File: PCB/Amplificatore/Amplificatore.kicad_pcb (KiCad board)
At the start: 2 copper layers, 11 parts, among them U2 ECC83

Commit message: avanzamento pcb
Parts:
- added C10: 680nF, Capacitor_THT:C_Rect_L18.0mm_W11.0mm_P15.00mm_FKS3_FKP3, F.Cu at (212.1, 97.6)
- added C11: 22nF, Capacitor_THT:C_Rect_L13.0mm_W4.0mm_P10.00mm_FKS3_FKP3_MKS4, F.Cu at (212.1, 112.2)
- added C5: 22nF, Capacitor_THT:C_Rect_L13.0mm_W4.0mm_P10.00mm_FKS3_FKP3_MKS4, F.Cu at (212.1, 106.7)
- added C7: 1nF, Capacitor_THT:C_Rect_L13.0mm_W4.0mm_P10.00mm_FKS3_FKP3_MKS4, F.Cu at (231.6, 94.1)
- added C8: 10uF, Capacitor_Tantalum_SMD:CP_EIA-3216-10_Kemet-I, F.Cu at (227.2, 110.0)
- added C9: 470pF, Capacitor_THT:C_Rect_L10.0mm_W3.0mm_P7.50mm_MKS4, F.Cu at (226.4, 106.2)
- added J1: POT-1, Connector_PinSocket_2.00mm:PinSocket_1x03_P2.00mm_Vertical, F.Cu at (237.9, 103.8)
- added R6: 100K, Resistor_SMD:R_2512_6332Metric, F.Cu at (233.7, 99.3)
- added R7: 1K5, Resistor_SMD:R_0805_2012Metric, F.Cu at (232.3, 109.9)
- added R8: 100K, Resistor_SMD:R_2512_6332Metric, F.Cu at (248.3, 93.8)
- added R9: 47K, Resistor_SMD:R_2512_6332Metric, F.Cu at (242.4, 99.3)
- renumbered C3 to C2, C5 to C3, C2 to C4, C4 to C6, R4 to R3, R3 to R4, U2 to U1
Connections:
- U1 pad 1: (no net) -> Net-(C11-Pad2)
- U1 pad 2: (no net) -> Net-(R6-Pad1)
- U1 pad 3: (no net) -> Net-(C10-Pad2)

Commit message: Add files via upload
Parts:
- added K1: G5Q-1, Relay_THT:Relay_SPDT_Omron-G5Q-1, F.Cu at (226.1, 73.7)
- added R10: 220K, Resistor_SMD:R_2512_6332Metric, F.Cu at (227.9, 78.6)
- added R11: 220K, Resistor_SMD:R_2512_6332Metric, F.Cu at (236.6, 78.6)
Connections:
- R4 pad 1: Net-(C2-Pad1) -> Net-(C6-Pad1)

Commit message: ...
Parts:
- added C12: 1nF, Capacitor_THT:C_Rect_L13.0mm_W4.0mm_P10.00mm_FKS3_FKP3_MKS4, F.Cu at (137.2, 73.7)
- added C13: 2n2F, Capacitor_THT:C_Rect_L13.0mm_W4.0mm_P10.00mm_FKS3_FKP3_MKS4, F.Cu at (130.8, 81.3)
- added C14: 100nF, Capacitor_THT:C_Rect_L18.0mm_W5.0mm_P15.00mm_FKS3_FKP3, F.Cu at (160.0, 82.5)
- added C15: 100nF, Capacitor_THT:C_Rect_L18.0mm_W5.0mm_P15.00mm_FKS3_FKP3, F.Cu at (181.6, 63.5)
- added C16: 100nF, Capacitor_THT:C_Rect_L18.0mm_W5.0mm_P15.00mm_FKS3_FKP3, F.Cu at (186.7, 50.8)
- added C17: 4n7F, Capacitor_THT:C_Rect_L13.0mm_W4.0mm_P10.00mm_FKS3_FKP3_MKS4, F.Cu at (186.7, 57.1)
- added C18: 10nF, Capacitor_THT:C_Rect_L13.0mm_W4.0mm_P10.00mm_FKS3_FKP3_MKS4, F.Cu at (221.0, 57.1)
- added C19: 220pF, Capacitor_THT:C_Rect_L7.2mm_W4.5mm_P5.00mm_FKS2_FKP2_MKS2_MKP2, F.Cu at (203.2, 64.8)
- added C20: 470pF, Capacitor_THT:C_Rect_L10.0mm_W3.0mm_P7.50mm_MKS4, F.Cu at (219.7, 63.5)
- added C21: 100nF, Capacitor_THT:C_Rect_L18.0mm_W5.0mm_P15.00mm_FKS3_FKP3, F.Cu at (210.8, 50.8)
- added C22: 2n2F, Capacitor_THT:C_Rect_L13.0mm_W4.0mm_P10.00mm_FKS3_FKP3_MKS4, F.Cu at (233.7, 69.8)
- added D1: 1N4007, Diode_THT:D_DO-41_SOD81_P10.16mm_Horizontal, F.Cu at (135.9, 58.4)
- added D2: 1N4007, Diode_THT:D_DO-41_SOD81_P10.16mm_Horizontal, F.Cu at (148.6, 58.4)
- added D3: 1N4007, Diode_THT:D_DO-41_SOD81_P10.16mm_Horizontal, F.Cu at (143.5, 73.7)
- added D4: 1N4007, Diode_THT:D_DO-41_SOD81_P10.16mm_Horizontal, F.Cu at (142.2, 48.3)
- added D5: 1N4007, Diode_THT:D_DO-41_SOD81_P10.16mm_Horizontal, F.Cu at (129.5, 48.3)
- added D6: 1N4007, Diode_THT:D_DO-41_SOD81_P10.16mm_Horizontal, F.Cu at (143.5, 81.3)
- added D7: 1N4007, Diode_THT:D_DO-41_SOD81_P10.16mm_Horizontal, F.Cu at (137.2, 91.4)
- added J10: POWER, Connector_Molex:Molex_KK-396_A-41791-0003_1x03_P3.96mm_Vertical, F.Cu at (109.2, 47.0)
- added J11: FILAMENT-U2, Connector_PinSocket_2.00mm:PinSocket_1x03_P2.00mm_Vertical, F.Cu at (166.4, 54.6)
- added J12: FILAMENT-U1, Connector_PinSocket_2.00mm:PinSocket_1x03_P2.00mm_Vertical, F.Cu at (99.1, 55.9)
- added J2: POT-LEAD, Connector_PinSocket_2.00mm:PinSocket_1x03_P2.00mm_Vertical, F.Cu at (129.5, 67.3)
- added J3: SEND-RETURN, Connector_PinSocket_2.00mm:PinSocket_1x03_P2.00mm_Vertical, F.Cu at (184.2, 76.2)
- added J4: In, Connector_PinSocket_2.00mm:PinSocket_1x03_P2.00mm_Vertical, F.Cu at (53.3, 64.8)
- added J5: POT-BASS-BACK, Connector_PinSocket_2.00mm:PinSocket_1x03_P2.00mm_Vertical, F.Cu at (193.0, 49.5)
- added J6: POT-MID, Connector_PinSocket_2.00mm:PinSocket_1x03_P2.00mm_Vertical, F.Cu at (214.6, 63.5)
- added J7: POT-TREBLE, Connector_PinSocket_2.00mm:PinSocket_1x03_P2.00mm_Vertical, F.Cu at (221.0, 72.4)
- added J8: POT-BASS-FRONT, Connector_PinSocket_2.00mm:PinSocket_1x03_P2.00mm_Vertical, F.Cu at (224.8, 78.7)
- added J9: MASTER, Connector_PinSocket_2.00mm:PinSocket_1x03_P2.00mm_Vertical, F.Cu at (224.8, 85.1)
- added K2: G5Q-1, Relay_THT:Relay_SPDT_Omron-G5Q-1, F.Cu at (102.9, 90.2)
- added K3: G5Q-1, Relay_THT:Relay_SPDT_Omron-G5Q-1, F.Cu at (190.5, 72.4)
- added K4: G5Q-1, Relay_THT:Relay_SPDT_Omron-G5Q-1, F.Cu at (204.5, 72.4)
- added R12: 10K, Resistor_SMD:R_2512_6332Metric, F.Cu at (151.1, 71.1)
- added R13: 100K, Resistor_SMD:R_2512_6332Metric, F.Cu at (151.1, 81.3)
- added R14: 47K, Resistor_SMD:R_2512_6332Metric, F.Cu at (152.4, 63.5)
- added R15: 1Meg, Resistor_SMD:R_0805_2012Metric, F.Cu at (158.8, 90.2)
- added R16: 1K5, Resistor_SMD:R_0805_2012Metric, F.Cu at (156.2, 58.4)
- added R17: 100K, Resistor_SMD:R_2512_6332Metric, B.Cu at (154.9, 50.8)
- added R18: 47K, Resistor_SMD:R_2512_6332Metric, F.Cu at (151.1, 90.2)
- added R19: 100K, Resistor_SMD:R_2512_6332Metric, F.Cu at (166.4, 90.2)
- added R20: 10K, Resistor_SMD:R_2512_6332Metric, F.Cu at (176.5, 90.2)
- added R21: 10R, Resistor_SMD:R_2512_6332Metric, F.Cu at (184.2, 88.1)
- added R22: 1Meg, Resistor_SMD:R_0805_2012Metric, B.Cu at (189.2, 63.5)
- added R23: 470R, Resistor_SMD:R_0805_2012Metric, F.Cu at (180.3, 74.6)
- added R24: 220K, Resistor_SMD:R_2512_6332Metric, F.Cu at (163.8, 48.3)
- added R25: 100K, Resistor_SMD:R_2512_6332Metric, F.Cu at (199.4, 52.1)
- added R26: 100K, Resistor_SMD:R_2512_6332Metric, F.Cu at (204.5, 52.1)
- added R27: 10K, Resistor_SMD:R_2512_6332Metric, F.Cu at (233.7, 52.1)
- added R28: 100K, Resistor_SMD:R_2512_6332Metric, F.Cu at (233.7, 77.5)
- added U2: ECC83, Valve:Valve_ECC-83-2, B.Cu at (171.4, 63.5)
- C8, R1, R3, R7, R9, U1: moved to B.Cu
- J1: value POT-1 -> POT-GAIN
- moved J1 186.7 mm to (53.3, 76.2), turned to 180 degrees
- moved C7 173.3 mm to (58.4, 88.9)
- moved R8 171.0 mm to (81.3, 57.1)
- moved C9 161.6 mm to (73.7, 53.3), turned to 180 degrees
- moved R6 159.2 mm to (74.9, 87.6), turned to 270 degrees
- moved C5 155.6 mm to (58.4, 82.5)
- moved R11 149.4 mm to (87.6, 90.2)
- moved R10 140.4 mm to (87.6, 83.8), turned to 180 degrees
- moved C4 133.8 mm to (58.4, 72.4)
- moved R9 132.7 mm to (110.5, 85.1), turned to 180 degrees
- moved R7 128.4 mm to (113.0, 62.2)
- moved C8 125.9 mm to (113.0, 57.1)
- moved K1 123.2 mm to (102.9, 76.2)
- moved C11 117.7 mm to (96.5, 90.2), turned to 90 degrees
- moved C1 105.1 mm to (58.4, 63.5), turned to 90 degrees
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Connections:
- net LEAD-SW-A renamed LEAD-SW
- net Net-(C5-Pad1) renamed /Mute
- C6 pad 1: Net-(C6-Pad1) -> /VCC
- C9 pad 2: Net-(C6-Pad1) -> Net-(C2-Pad1)
- K1 pad 2: Net-(K1-Pad2) -> GND
- K1 pad 5: LEAD-SW-B -> COMMON
- R4 pad 1: Net-(C6-Pad1) -> Net-(C2-Pad1)
- R5 pad 1: Net-(C6-Pad1) -> /VCC
- R8 pad 1: Net-(C6-Pad1) -> Net-(C2-Pad1)
- U1 pad 4: (no net) -> Net-(J12-Pad1)
- U1 pad 5: (no net) -> Net-(J12-Pad2)
- U1 pad 9: (no net) -> Net-(J12-Pad3)

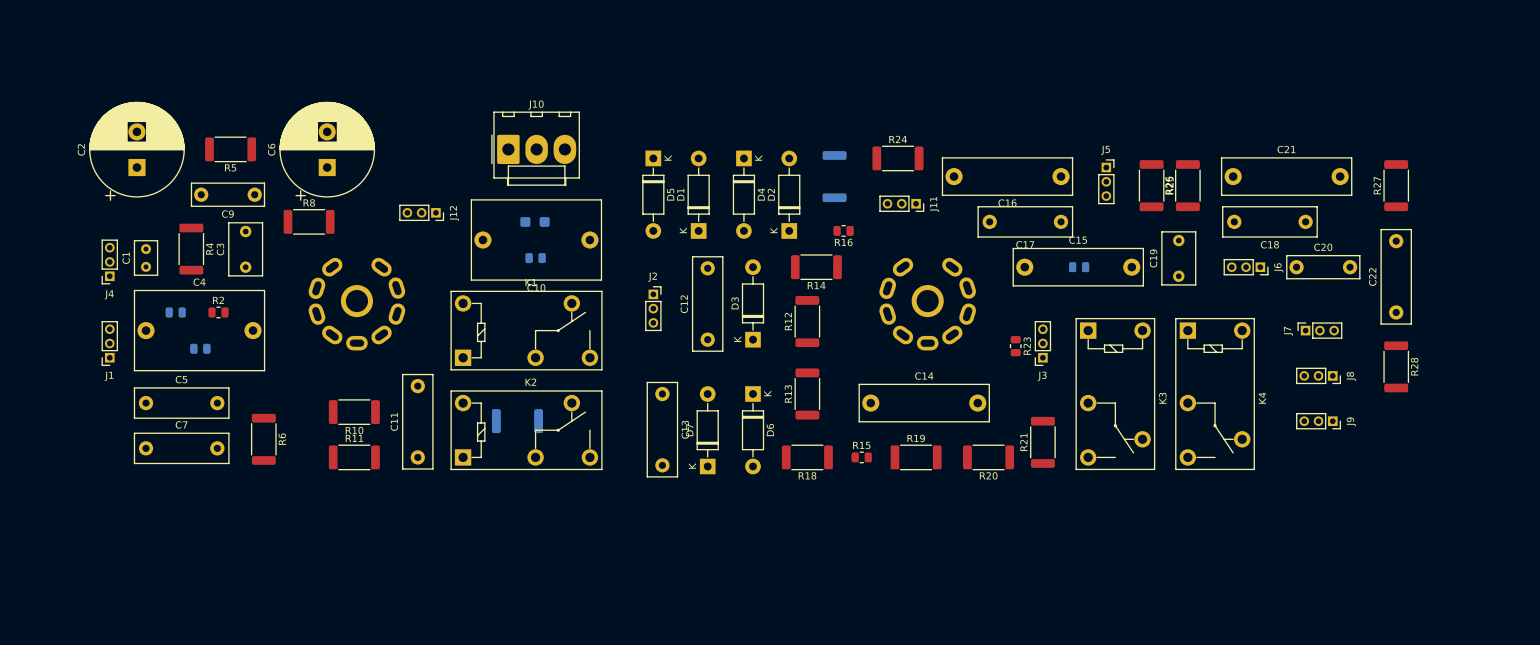
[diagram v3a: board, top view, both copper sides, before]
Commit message: sbrogliato pcb pre-ampli
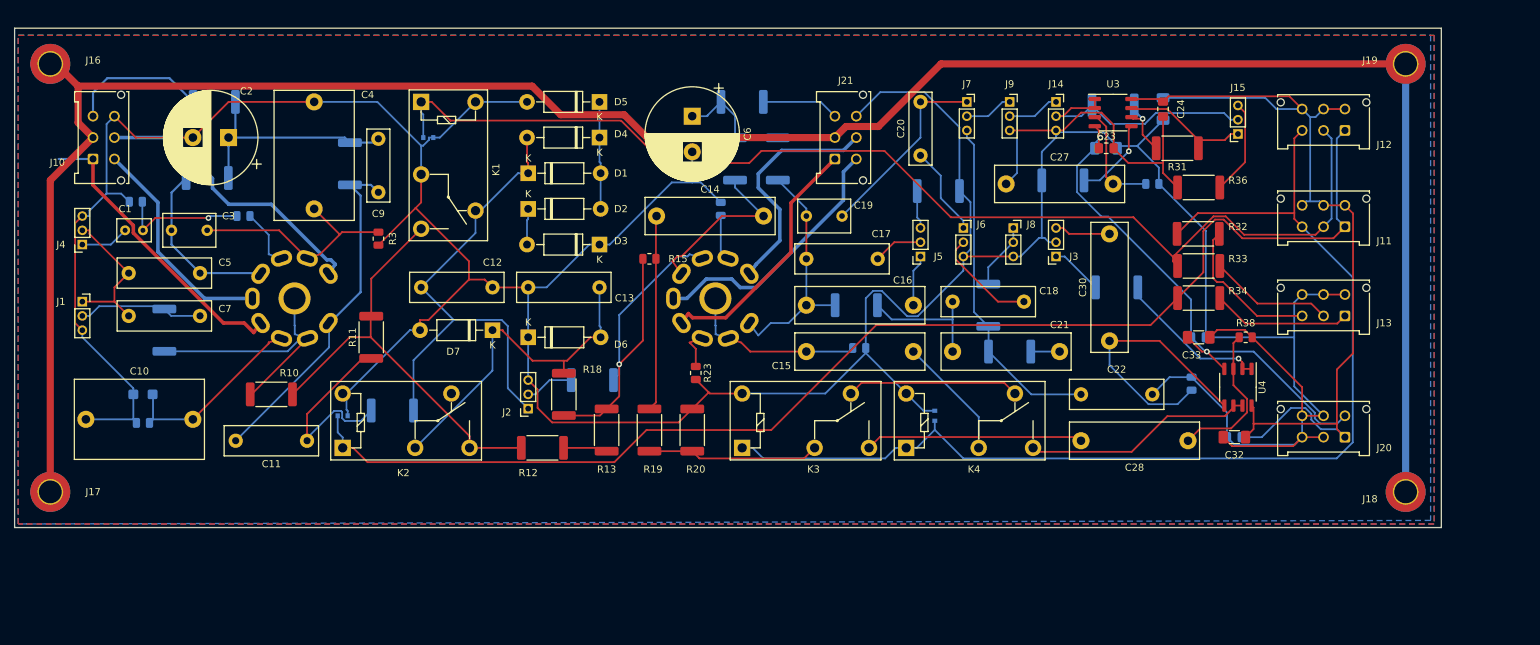
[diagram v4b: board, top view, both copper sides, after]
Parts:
- added C23: 100nF, Capacitor_SMD:C_0805_2012Metric_Pad1.18x1.45mm_HandSolder, F.Cu at (193.0, 46.8)
- added C24: 100nF, Capacitor_SMD:C_0805_2012Metric_Pad1.18x1.45mm_HandSolder, F.Cu at (201.0, 41.3)
- added C25: 1uF, Capacitor_SMD:C_1206_3216Metric_Pad1.33x1.80mm_HandSolder, B.Cu at (201.0, 41.3)
- added C26: 1uF, Capacitor_SMD:C_1206_3216Metric_Pad1.33x1.80mm_HandSolder, B.Cu at (193.0, 46.8)
- added C27: 100nF, Capacitor_THT:C_Rect_L18.0mm_W5.0mm_P15.00mm_FKS3_FKP3, F.Cu at (179.0, 51.8)
- added C28: 100nF, Capacitor_THT:C_Rect_L18.0mm_W5.0mm_P15.00mm_FKS3_FKP3, F.Cu at (204.5, 87.8)
- added C29: 100nF, Capacitor_SMD:C_0805_2012Metric_Pad1.18x1.45mm_HandSolder, B.Cu at (206.0, 73.3)
- added C30: 100nF, Capacitor_THT:C_Rect_L18.0mm_W5.0mm_P15.00mm_FKS3_FKP3, F.Cu at (193.5, 73.8)
- added C31: 100nF, Capacitor_SMD:C_0805_2012Metric_Pad1.18x1.45mm_HandSolder, B.Cu at (211.0, 87.3)
- added C32: 1uF, Capacitor_SMD:C_1206_3216Metric_Pad1.33x1.80mm_HandSolder, F.Cu at (211.0, 87.3)
- added C33: 1uF, Capacitor_SMD:C_1206_3216Metric_Pad1.33x1.80mm_HandSolder, F.Cu at (206.0, 73.3)
- added D10: 1N4148WT, Diode_SMD:D_SOD-523, B.Cu at (169.0, 84.3)
- added D8: 1N4148WT, Diode_SMD:D_SOD-523, B.Cu at (86.0, 84.3)
- added D9: 1N4148WT, Diode_SMD:D_SOD-523, B.Cu at (98.0, 45.3)
- added J13: LED_SWITCHES, Connector_Molex:Molex_Micro-Fit_3.0_43045-0612_2x03_P3.00mm_Vertical, F.Cu at (226.5, 70.3)
- added J14: POWER-STAGE, Connector_PinSocket_2.00mm:PinSocket_1x03_P2.00mm_Vertical, F.Cu at (186.0, 40.3)
- added J15: LINE-OUT, Connector_PinSocket_2.00mm:PinSocket_1x03_P2.00mm_Vertical, F.Cu at (211.5, 44.8)
- added J16: Conn_01x01, MountingHole:MountingHole_3.2mm_M3_DIN965_Pad_TopBottom, F.Cu at (45.0, 35.0)
- added J17: Conn_01x01, MountingHole:MountingHole_3.2mm_M3_DIN965_Pad_TopBottom, F.Cu at (45.0, 95.0)
- added J18: Conn_01x01, MountingHole:MountingHole_3.2mm_M3_DIN965_Pad_TopBottom, F.Cu at (235.0, 95.0)
- added J19: Conn_01x01, MountingHole:MountingHole_3.2mm_M3_DIN965_Pad_TopBottom, F.Cu at (235.0, 35.0)
- added J20: PWR_DC, Connector_Molex:Molex_Micro-Fit_3.0_43045-0612_2x03_P3.00mm_Vertical, F.Cu at (226.5, 87.3)
- added J21: PWR_VALVE2, Connector_Molex:Molex_Micro-Fit_3.0_43045-0612_2x03_P3.00mm_Vertical, F.Cu at (155.0, 48.3)
- added R29: 100K, Resistor_SMD:R_2512_6332Metric, B.Cu at (194.0, 40.8)
- added R30: 10K, Resistor_SMD:R_2512_6332Metric, B.Cu at (187.0, 51.3)
- added R31: 10K, Resistor_SMD:R_2512_6332Metric, F.Cu at (203.0, 46.8)
- added R32: 1K, Resistor_SMD:R_2512_6332Metric, F.Cu at (205.9, 58.8)
- added R33: 1K, Resistor_SMD:R_2512_6332Metric, F.Cu at (206.0, 63.3)
- added R34: 1K, Resistor_SMD:R_2512_6332Metric, F.Cu at (206.0, 67.8)
- added R35: 1Meg, Resistor_SMD:R_0805_2012Metric, B.Cu at (199.5, 51.8)
- added R36: 10R, Resistor_SMD:R_2512_6332Metric, F.Cu at (206.0, 52.3)
- added R37: 10K, Resistor_SMD:R_2512_6332Metric, B.Cu at (68.0, 40.3)
- added R38: 1Meg, Resistor_SMD:R_0805_2012Metric, F.Cu at (212.6, 73.3)
- added R39: 1Meg, Resistor_SMD:R_0805_2012Metric, B.Cu at (205.0, 79.8)
- added U3: TL082, Package_SO:SO-8_3.9x4.9mm_P1.27mm, F.Cu at (194.0, 41.8)
- added U4: TL082, Package_SO:SO-8_3.9x4.9mm_P1.27mm, F.Cu at (211.5, 80.3)
- J10: value POWER -> PWR_VALVE1; footprint Connector_Molex:Molex_KK-396_A-41791-0003_1x03_P3.96mm_Vertical -> Connector_Molex:Molex_Micro-Fit_3.0_43045-0612_2x03_P3.00mm_Vertical
- J11: value FILAMENT-U2 -> LOCAL_SWITCHES; footprint Connector_PinSocket_2.00mm:PinSocket_1x03_P2.00mm_Vertical -> Connector_Molex:Molex_Micro-Fit_3.0_43045-0612_2x03_P3.00mm_Vertical
- J12: value FILAMENT-U1 -> REMOTE_SWITCHES; footprint Connector_PinSocket_2.00mm:PinSocket_1x03_P2.00mm_Vertical -> Connector_Molex:Molex_Micro-Fit_3.0_43045-0612_2x03_P3.00mm_Vertical
- R14, R16, R2, R21, R24, R25, R26, R27, R28, R4, R5, R6, R8: moved to B.Cu
- R3: moved to F.Cu
- moved J12 128.0 mm to (226.5, 44.3), turned to 180 degrees
- moved C10 75.0 mm to (50.0, 84.8), turned to 0 degrees
- moved R5 72.0 mm to (142.0, 40.3), turned to 0 degrees
- moved J9 63.7 mm to (179.5, 40.3), turned to 0 degrees
- moved J11 60.2 mm to (226.5, 57.8), turned to 180 degrees
- moved C8 60.0 mm to (58.0, 81.3), turned to 180 degrees
- moved R7 59.7 mm to (58.0, 85.3), turned to 180 degrees
- moved R27 59.0 mm to (179.5, 75.3), turned to 0 degrees
- moved J10 58.2 mm to (51.0, 48.3), turned to 90 degrees
- moved R28 57.8 mm to (176.5, 68.8), turned to 90 degrees
- moved J7 57.3 mm to (173.5, 40.3), turned to 0 degrees
- moved C20 55.0 mm to (167.0, 47.8), turned to 90 degrees
- moved C6 51.7 mm to (135.0, 42.3), turned to 270 degrees
- moved K3 51.2 mm to (142.0, 88.8), turned to 0 degrees
- moved R26 49.4 mm to (158.0, 68.8), turned to 0 degrees
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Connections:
- C6 pad 1: /VCC -> /VCC2_B
- J10 pad 1: /VCC -> Net-(J10-Pad1)
- J10 pad 3: GND -> /VCC1
- J11 pad 1: Net-(J11-Pad1) -> /RITHM-SW
- J11 pad 2: Net-(J11-Pad2) -> /LEAD_SW
- J11 pad 3: Net-(J11-Pad3) -> /SR_SW
- J12 pad 1: Net-(J12-Pad1) -> /RITHM-SW
- J12 pad 2: Net-(J12-Pad2) -> /LEAD_SW
- J12 pad 3: Net-(J12-Pad3) -> /SR_SW
- J3 pad 2: Net-(J3-Pad2) -> GND
- J3 pad 3: Net-(J3-Pad3) -> Net-(C30-Pad2)
- K1 pad 1: LEAD-SW -> /LEAD_SW
- K1 pad 3: Net-(C12-Pad2) -> Net-(K1-Pad3)
- K1 pad 4: Net-(K1-Pad4) -> Net-(C12-Pad2)
- K1 pad 5: COMMON -> GND
- K2 pad 1: RITHM-SW -> /RITHM-SW
- K2 pad 3: Net-(K1-Pad4) -> Net-(K1-Pad3)
- K2 pad 4: Net-(K2-Pad4) -> (no net)
- K2 pad 5: COMMON -> GND
- K3 pad 1: SEND-SW -> /SR_SW
- K3 pad 3: Net-(J3-Pad3) -> Net-(C28-Pad2)
- K3 pad 5: COMMON -> GND
- K4 pad 1: SEND-SW -> /SR_SW
- K4 pad 3: Net-(J3-Pad1) -> Net-(K4-Pad3)
- K4 pad 5: COMMON -> GND
- R10 pad 1: Net-(K1-Pad4) -> Net-(K1-Pad3)
- R11 pad 2: Net-(K1-Pad4) -> Net-(K1-Pad3)
- R12 pad 2: Net-(K1-Pad4) -> Net-(K1-Pad3)
- R17 pad 1: /VCC -> /VCC2_B
- R21 pad 1: GND -> Net-(R21-Pad1)
- R21 pad 2: Net-(J3-Pad2) -> Net-(J3-Pad1)
- R24 pad 1: /VCC -> /VCC2_B
- R5 pad 1: /VCC -> /VCC2_B
- R5 pad 2: Net-(C2-Pad1) -> /VCC2
- U1 pad 4: Net-(J12-Pad1) -> Net-(J10-Pad1)
- U1 pad 5: Net-(J12-Pad2) -> Net-(J10-Pad4)
- U1 pad 9: Net-(J12-Pad3) -> Net-(J10-Pad5)
- U2 pad 4: Net-(J11-Pad1) -> Net-(J21-Pad1)
- U2 pad 5: Net-(J11-Pad2) -> Net-(J21-Pad4)
- U2 pad 9: Net-(J11-Pad3) -> Net-(J21-Pad5)
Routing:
- net GND: track 0.00 -> 605.2 mm
- net Earth: track 0.00 -> 318.8 mm
- net /RITHM-SW: track 0.00 -> 179.8 mm
- net /LEAD_SW: track 0.00 -> 161.9 mm
- net /SR_SW: track 0.00 -> 156.9 mm
- net /VDD: track 0.00 -> 139.9 mm
- net /VEE: track 0.00 -> 74.6 mm, vias 0 -> 2
- net Net-(C12-Pad2): track 0.00 -> 70.7 mm
- net Net-(K1-Pad3): track 0.00 -> 60.9 mm
- net Net-(R13-Pad1): track 0.00 -> 54.3 mm, vias 0 -> 1
- net Net-(C11-Pad2): track 0.00 -> 49.1 mm
- net Net-(C13-Pad2): track 0.00 -> 48.2 mm
- net Net-(C22-Pad2): track 0.00 -> 47.7 mm
- net Net-(J10-Pad1): track 0.00 -> 41.8 mm
- net Net-(J10-Pad5): track 0.00 -> 40.8 mm
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- added copper zone on B.Cu, net GND
- added copper zone on F.Cu, net GND
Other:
- board outline added: 200 x 70 mm
